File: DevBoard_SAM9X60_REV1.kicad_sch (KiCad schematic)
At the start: 11 parts, among them U101 SAM9X60-V/DWB, U105 W9751G6NB-25, Y102 Crystal_GND24

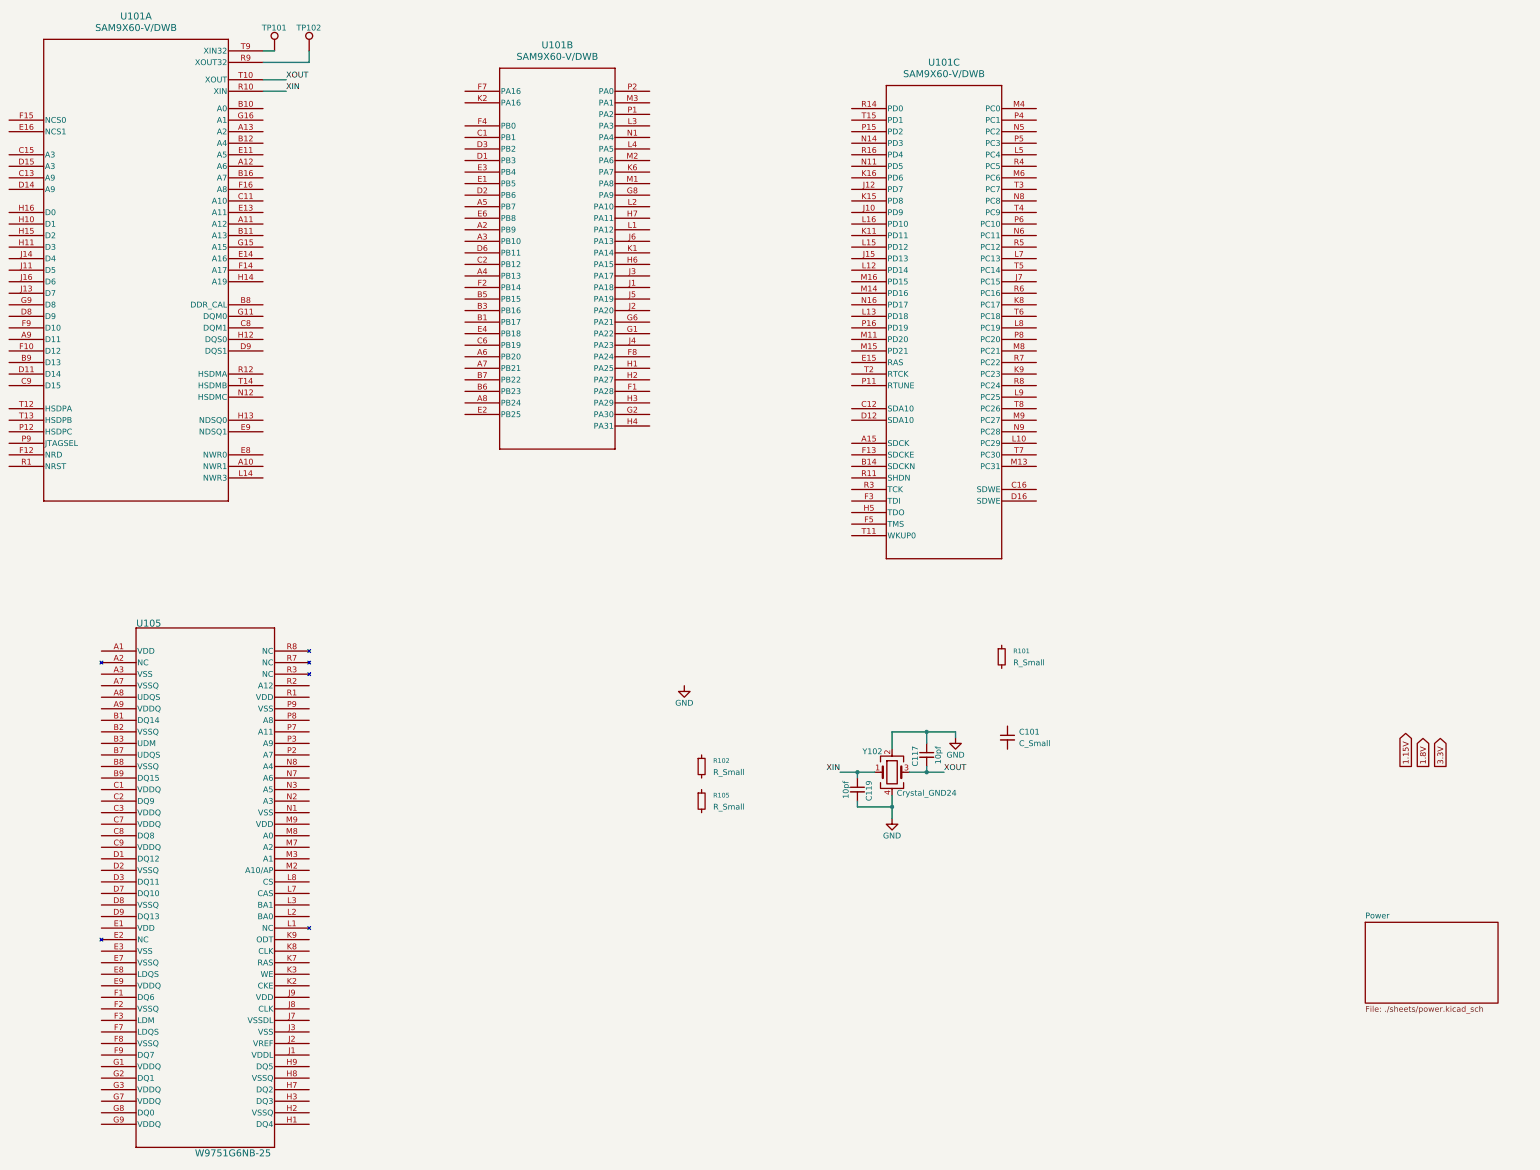
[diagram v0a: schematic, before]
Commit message: Update power schematic
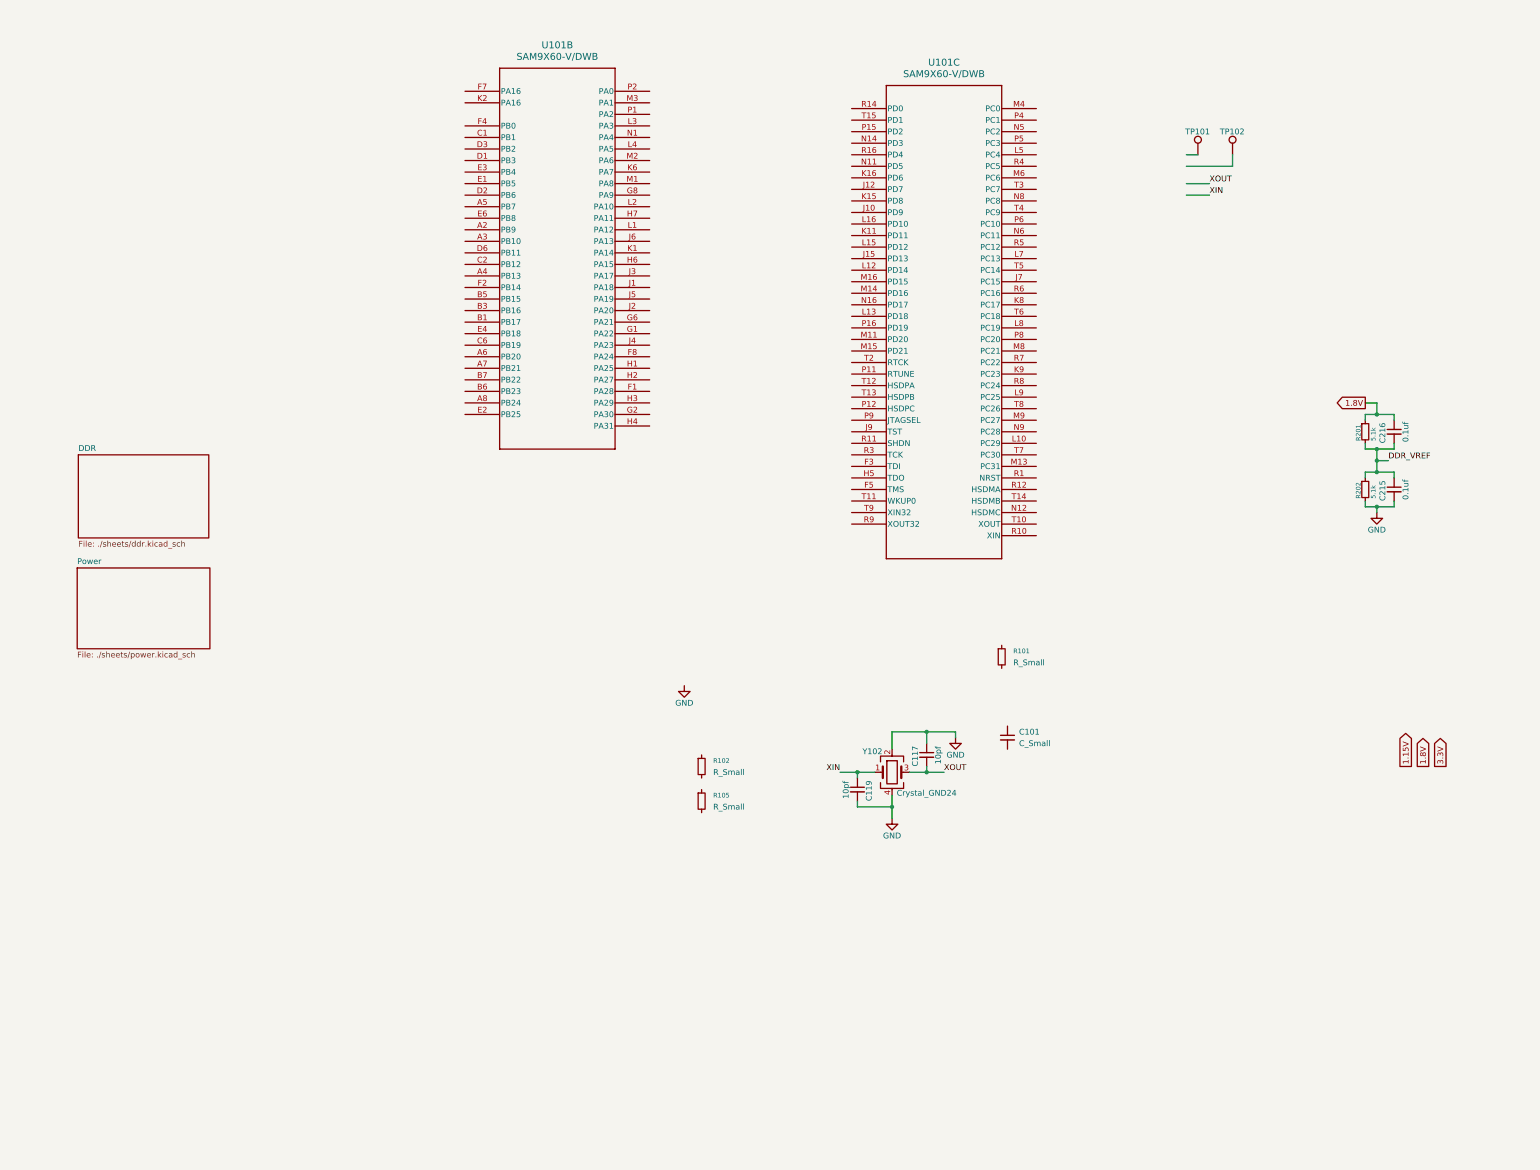
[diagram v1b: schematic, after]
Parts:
- removed unit 1 of U101
- removed U105: W9751G6NB-25, W9751G6NB-25:BGA_6NB-25_WIN, symbol W9751G6NB-25:W9751G6NB-25
- added C215, C216: 0.1uf, Capacitor_SMD:C_0603_1608Metric_Pad1.08x0.95mm_HandSolder, symbol Device:C_Small
- added R201, R202: 5.1k, Resistor_SMD:R_0603_1608Metric_Pad0.98x0.95mm_HandSolder, symbol Device:R_Small
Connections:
- net 1.8V: now also C216.1, R201.1
- net GND: now also C215.2, R202.2
- new net DDR_VREF: C215.1, C216.2, R201.2, R202.1
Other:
- added sheet DDR (./sheets/ddr.kicad_sch)
- moved on the sheet: TP101, TP102

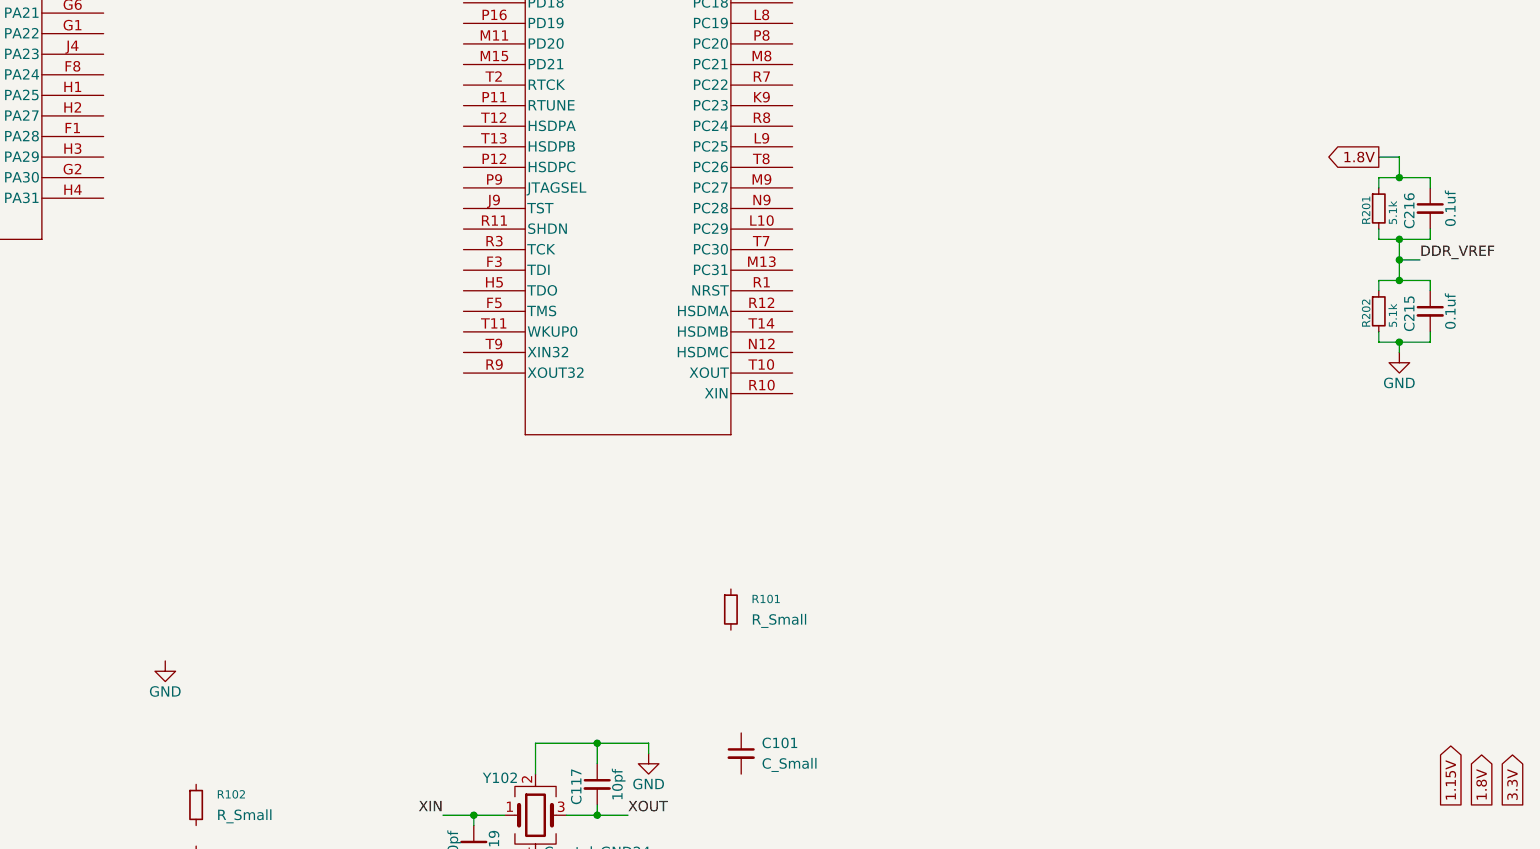
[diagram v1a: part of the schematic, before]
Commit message: Finish DRAM schematic
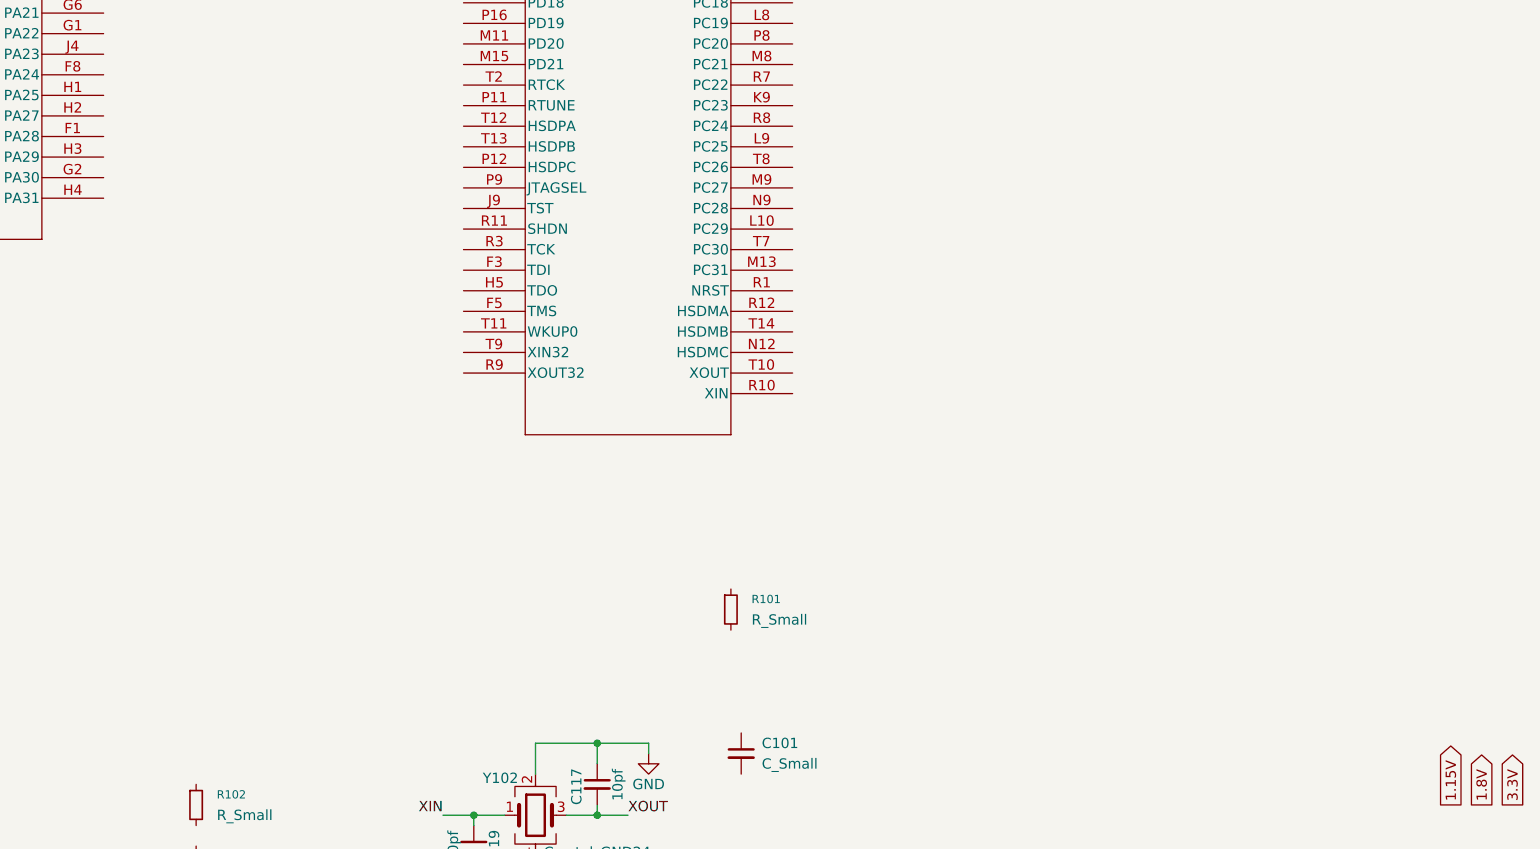
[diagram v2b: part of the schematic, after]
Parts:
- removed C215, C216: 0.1uf, Capacitor_SMD:C_0603_1608Metric_Pad1.08x0.95mm_HandSolder, symbol Device:C_Small
- removed R201, R202: 5.1k, Resistor_SMD:R_0603_1608Metric_Pad0.98x0.95mm_HandSolder, symbol Device:R_Small

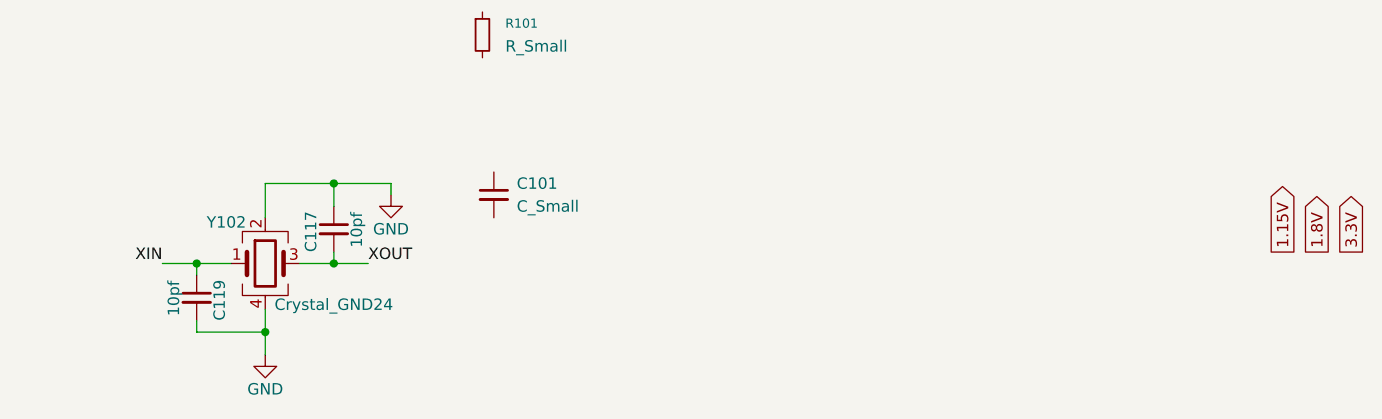
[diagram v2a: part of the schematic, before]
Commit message: Update schematic
- Update VDDCORE to 1.13V
- Fix DDR_CAL circuit
- Update external load capacitor to 22pf
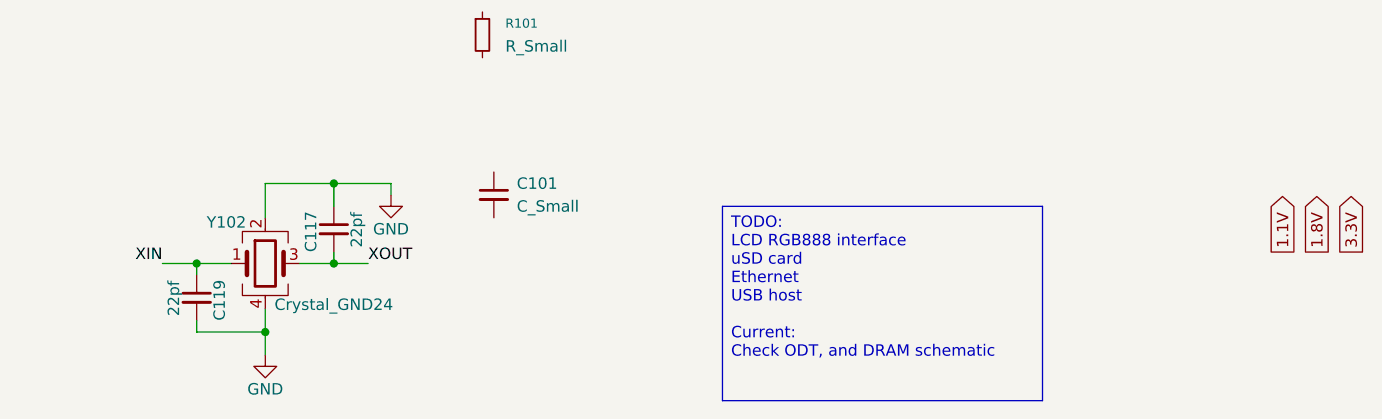
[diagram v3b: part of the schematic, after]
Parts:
- C117, C119: value 10pf -> 22pf
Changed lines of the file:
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@@
 		(company "ssDhp")
+	)
+	(text_box "TODO:\nLCD RGB888 interface\nuSD card\nEthernet\nUSB host\n\nCurrent: \nCheck ODT, and DRAM schematic\n"
+		(exclude_from_sim no)
+		(at 288.29 185.42 0)
+		(size 35.56 21.59)
+		(margins 0.9525 0.9525 0.9525 0.9525)
+		(stroke
+			(width 0)
+			(type solid)
+		)
+		(fill
+			(type none)
+		)
+		(effects
+			(font
+				(size 1.27 1.27)
+			)
+			(justify left top)
+		)
 	)
 	(junction
@@
 		)
 	)
-	(global_label "1.15V"
+	(global_label "1.1V"
 		(shape output)
 		(at 350.52 190.5 90)
@@
 		)
 		(property "Intersheetrefs" "${INTERSHEET_REFS}"
-			(at 350.52 182.1929 90)
+			(at 350.52 183.4024 90)
 			(effects
 				(font
@@
 			)
 		)
-		(property "Value" "10pf"
+		(property "Value" "22pf"
 			(at 247.65 189.992 90)
 			(effects
@@
 			)
 		)
-		(property "Value" "10pf"
+		(property "Value" "22pf"
 			(at 227.33 197.612 90)
 			(effects
